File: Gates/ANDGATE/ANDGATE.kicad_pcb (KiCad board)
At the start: 2 copper layers, 53.3 x 20.3 mm, 14 parts, among them J1 Conn_01x01_Socket, J2 Conn_01x01_Socket, J3 Conn_01x03_Socket, U1 SN74LVC1G32DBVR

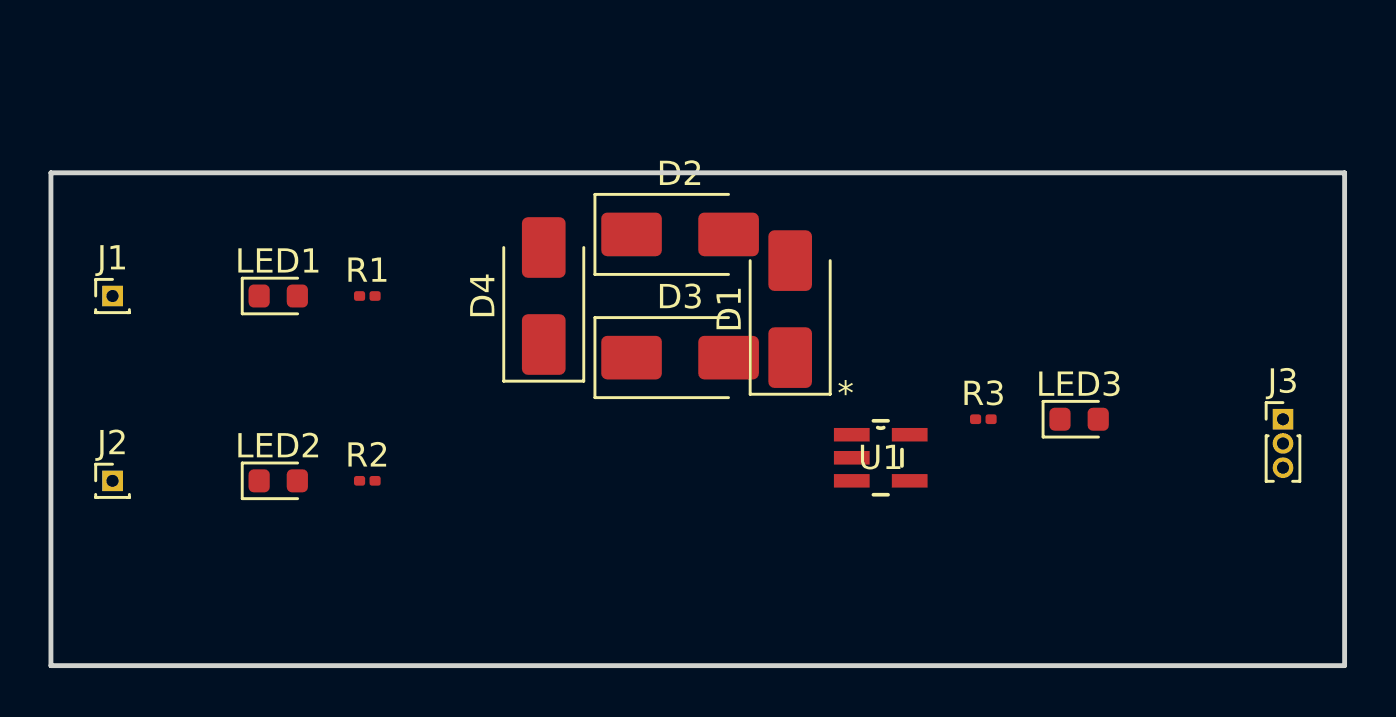
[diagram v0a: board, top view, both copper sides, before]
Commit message: AND GATE passes DRC but with silk screen warnings
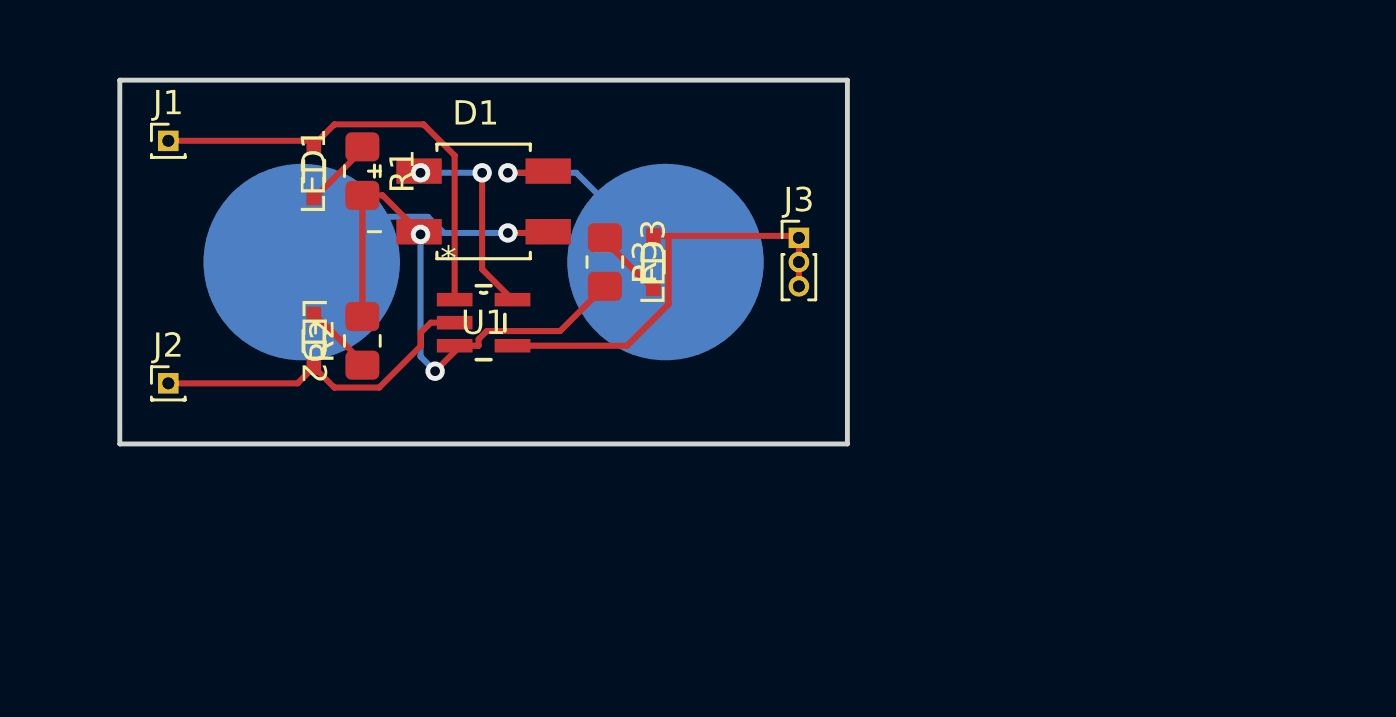
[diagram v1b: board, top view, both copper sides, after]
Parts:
- removed D2, D3, D4: 1N4004, Diode_SMD:D_SMA
- added J4: ~, DigitalLogicFootprints:8mm-snap, B.Cu at (147.5, 87.5)
- added J5: ~, DigitalLogicFootprints:8mm-snap, B.Cu at (162.5, 87.5)
- D1: value 1N4004 -> MB10F-13; footprint Diode_SMD:D_SMA -> DigitalLogicFootprints:DIOB_MB10F-13
- LED1, LED2, LED3: footprint LED_SMD:LED_0603_1608Metric -> DigitalLogicFootprints:LED_LTST-S220GKT_LTO
- R1, R2, R3: footprint Resistor_SMD:R_0201_0603Metric -> Resistor_SMD:R_0805_2012Metric_Pad1.20x1.40mm_HandSolder
- moved J3 21.3 mm to (168.0, 86.5)
- moved LED3 18.7 mm to (162.0, 87.5), turned to 90 degrees
- moved U1 17.3 mm to (155.0, 90.0)
- moved R3 16.9 mm to (160.0, 87.5), turned to -90 degrees
- moved D1 13.4 mm to (155.0, 85.0), turned to 0 degrees
- moved J1 6.80 mm to (142.0, 82.5)
- moved LED2 5.95 mm to (148.0, 90.8), turned to -90 degrees
- moved R2 5.77 mm to (150.0, 90.8), turned to 90 degrees
- moved LED1 5.36 mm to (148.0, 83.8), turned to 90 degrees
- moved R1 5.15 mm to (150.0, 83.8), turned to -90 degrees
- moved J2 4.63 mm to (142.0, 92.5)
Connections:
- D1 pad 1: Net-(D1-K) -> VCC
- D1 pad 2: VCC -> Net-(J5-PWR)
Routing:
- net GND: track 0.00 -> 23.1 mm, vias 0 -> 2
- net Net-(J3-Pin_1): track 0.00 -> 18.9 mm
- net Net-(J1-Pin_1): track 0.00 -> 18.7 mm
- net Net-(J2-Pin_1): track 0.00 -> 13.9 mm
- net Net-(J4-PWR): track 0.00 -> 11.3 mm, vias 0 -> 1
- net Net-(J5-PWR): track 0.00 -> 9.72 mm, vias 0 -> 1
- net VCC: track 0.00 -> 8.29 mm, vias 0 -> 2
- net Net-(LED3-Pad1): track 0.00 -> 2.94 mm
- net Net-(LED2-Pad1): track 0.00 -> 2.94 mm
- net Net-(LED1-Pad1): track 0.00 -> 2.94 mm
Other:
- board size 53.3 x 20.3 mm -> 30 x 15 mm

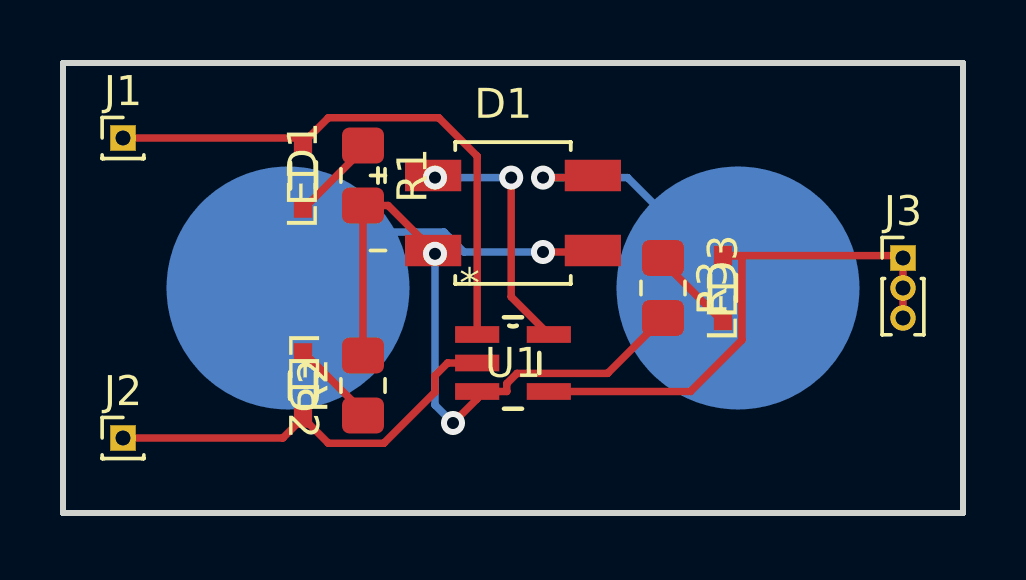
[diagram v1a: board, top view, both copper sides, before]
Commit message: Added mounting holes
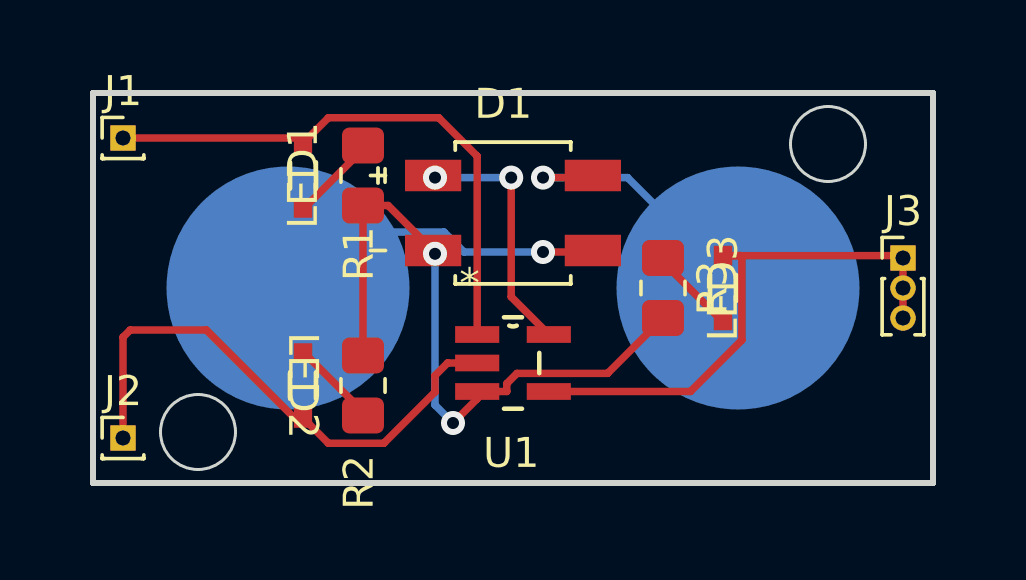
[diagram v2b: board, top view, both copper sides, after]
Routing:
- net Net-(J2-Pin_1): track 13.9 -> 18.3 mm
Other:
- board size 30 x 15 mm -> 28 x 13 mm
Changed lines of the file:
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@@
     (property "ki_keywords" "R res resistor")
     (attr smd)
-    (fp_text reference "R1" (at 0 -1.65 90) (layer "F.SilkS")
-        (effects (font (size 1 1) (thickness 0.15)))
-    )
-    (fp_text value "4k" (at 0 1.65 90) (layer "F.Fab")
+    (fp_text reference "R1" (at 2.61 0.14 90) (layer "F.SilkS")
+        (effects (font (size 1 1) (thickness 0.15)))
+    )
+    (fp_text value "4k" (at -5.01 0.14 90) (layer "F.Fab")
         (effects (font (size 1 1) (thickness 0.15)))
     )
@@
     (property "ki_keywords" "R res resistor")
     (attr smd)
-    (fp_text reference "R2" (at 0 -1.65 90) (layer "F.SilkS")
-        (effects (font (size 1 1) (thickness 0.15)))
-    )
-    (fp_text value "4k" (at 0 1.65 90) (layer "F.Fab")
+    (fp_text reference "R2" (at -3.23 -0.14 90) (layer "F.SilkS")
+        (effects (font (size 1 1) (thickness 0.15)))
+    )
+    (fp_text value "4k" (at 1.85 -0.14 90) (layer "F.Fab")
         (effects (font (size 1 1) (thickness 0.15)))
     )
@@
     (property "ki_keywords" "SN74LVC1G32DBVR")
     (attr smd)
-    (fp_text reference "U1" (at 0 0 unlocked) (layer "F.SilkS")
-        (effects (font (size 1 1) (thickness 0.15)))
-    )
-    (fp_text value "SN74LVC1G32DBVR" (at 0 0 unlocked) (layer "F.Fab")
+    (fp_text reference "U1" (at -0.06 3 unlocked) (layer "F.SilkS")
+        (effects (font (size 1 1) (thickness 0.15)))
+    )
+    (fp_text value "SN74LVC1G32DBVR" (at -0.06 6.52 unlocked) (layer "F.Fab")
         (effects (font (size 1 1) (thickness 0.15)))
     )
@@
     )
     (fp_text user "*" (at -1.4478 -2.6518 unlocked) (layer "F.Fab")
-        (effects (font (size 1 1) (thickness 0.15)))
-    )
-    (fp_text user "${REFERENCE}" (at 0 0 unlocked) (layer "F.Fab")
         (effects (font (size 1 1) (thickness 0.15)))
     )
@@
       (net 9 "Net-(J5-PWR)") (pinfunction "PWR") (pintype "output"))
   )
-  (gr_rect locked (start 140 80) (end 170 95)
+  (gr_circle (center 165.1 81.28) (end 165.1 81.28)
+    (stroke (width 0.1) (type default)) (fill none) (layer "Edge.Cuts"))
+  (gr_rect locked (start 141 81) (end 169 94)
     (stroke (width 0.2) (type default)) (fill none) (layer "Edge.Cuts"))
+  (gr_circle (center 165.5 82.7) (end 166.75 82.7)
+    (stroke (width 0.1) (type default)) (fill none) (layer "Edge.Cuts"))
+  (gr_circle (center 144.5 92.3) (end 145.75 92.3)
+    (stroke (width 0.1) (type default)) (fill none) (layer "Edge.Cuts"))
   (segment (start 150 84.75) (end 150 89.75) (width 0.25) (layer "F.Cu") (net 1))
   (segment (start 152.4475 86.36) (end 150.8375 84.75) (width 0.25) (layer "F.Cu") (net 1))
@@
   (via (at 153 92) (size 0.8) (drill 0.4) (layers "F.Cu" "B.Cu") (free) (net 1))
   (via (at 152.4 86.36) (size 0.8) (drill 0.4) (layers "F.Cu" "B.Cu") (net 1))
-  (segment (start 153 92) (end 152.4 91.4) (width 0.25) (layer "B.Cu") (net 1))
-  (segment (start 152.4 91.4) (end 152.4 86.36) (width 0.25) (layer "B.Cu") (net 1))
+  (segment (start 152.4 91.4) (end 153 92) (width 0.25) (layer "B.Cu") (net 1))
+  (segment (start 152.4 86.36) (end 152.4 91.4) (width 0.25) (layer "B.Cu") (net 1))
   (segment (start 154.94 87.796199) (end 154.94 83.82) (width 0.25) (layer "F.Cu") (net 2))
   (segment (start 156.1938 89.049999) (end 154.94 87.796199) (width 0.25) (layer "F.Cu") (net 2))
@@
   (segment (start 142 82.5) (end 147.8295 82.5) (width 0.25) (layer "F.Cu") (net 6))
   (segment (start 148 82.6705) (end 148.8455 81.825) (width 0.25) (layer "F.Cu") (net 6))
+  (segment (start 147.7095 91.8295) (end 148 91.8295) (width 0.25) (layer "F.Cu") (net 7))
+  (segment (start 147.7095 91.8295) (end 144.78 88.9) (width 0.25) (layer "F.Cu") (net 7))
   (segment (start 152.4 90.4196) (end 152.4 90.9701) (width 0.25) (layer "F.Cu") (net 7))
   (segment (start 152.4 90.9701) (end 150.6951 92.675) (width 0.25) (layer "F.Cu") (net 7))
+  (segment (start 142 89.14) (end 142 92.5) (width 0.25) (layer "F.Cu") (net 7))
   (segment (start 153.8062 90) (end 152.8196 90) (width 0.25) (layer "F.Cu") (net 7))
   (segment (start 152.8196 90) (end 152.4 90.4196) (width 0.25) (layer "F.Cu") (net 7))
-  (segment (start 147.3295 92.5) (end 148 91.8295) (width 0.25) (layer "F.Cu") (net 7))
   (segment (start 148.8455 92.675) (end 148 91.8295) (width 0.25) (layer "F.Cu") (net 7))
   (segment (start 150.6951 92.675) (end 148.8455 92.675) (width 0.25) (layer "F.Cu") (net 7))
-  (segment (start 142 92.5) (end 147.3295 92.5) (width 0.25) (layer "F.Cu") (net 7))
+  (segment (start 142.24 88.9) (end 142 89.14) (width 0.25) (layer "F.Cu") (net 7))
+  (segment (start 144.78 88.9) (end 142.24 88.9) (width 0.25) (layer "F.Cu") (net 7))
   (segment (start 160.914499 90.950001) (end 156.1938 90.950001) (width 0.25) (layer "F.Cu") (net 8))
   (segment (start 162.6298 86.4955) (end 162.6298 89.2347) (width 0.25) (layer "F.Cu") (net 8))

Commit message: Added HBB logo
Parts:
- added G***: LOGO, DigitalLogicFootprints:HBBLogo, F.Cu at (167.0, 93.0)

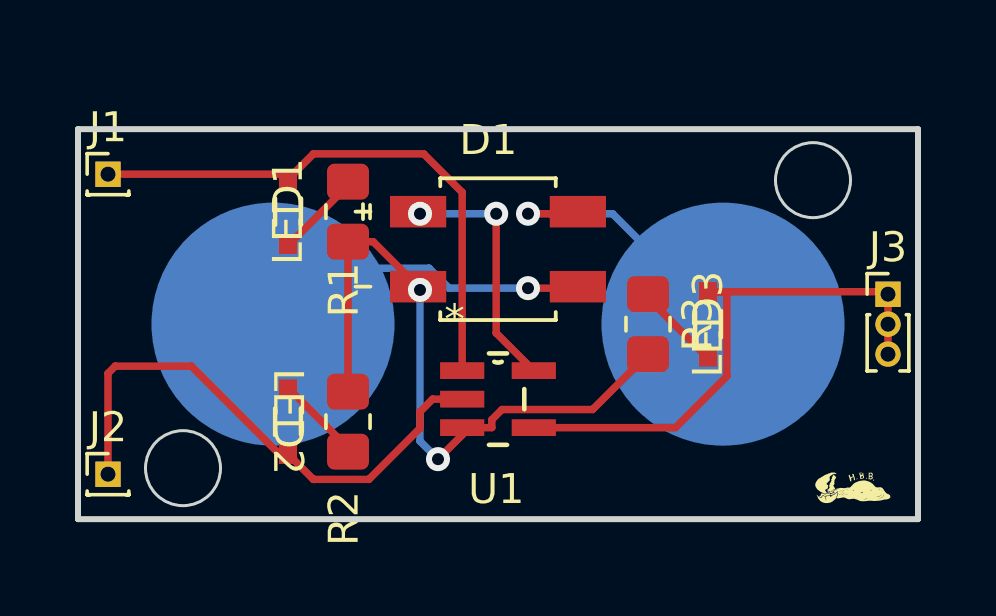
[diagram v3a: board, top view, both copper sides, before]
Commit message: Changed pins to 2.54mm from 1mm
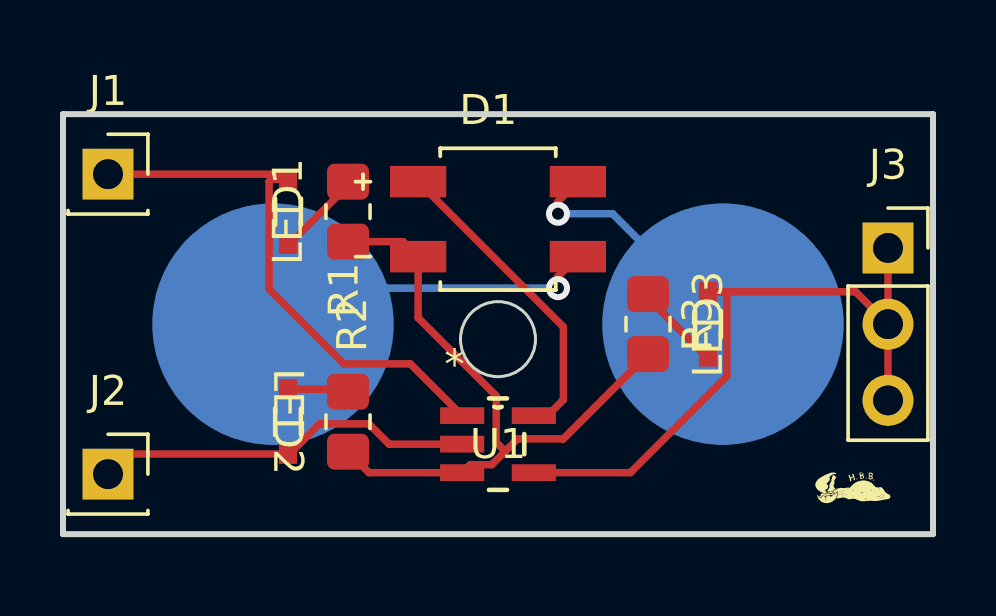
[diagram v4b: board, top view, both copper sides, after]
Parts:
- J1, J2: footprint Connector_PinHeader_1.00mm:PinHeader_1x01_P1.00mm_Vertical -> Connector_PinSocket_2.54mm:PinSocket_1x01_P2.54mm_Vertical
- J3: footprint Connector_PinHeader_1.00mm:PinHeader_1x03_P1.00mm_Vertical -> Connector_PinSocket_2.54mm:PinSocket_1x03_P2.54mm_Vertical
- moved J3 1.54 mm to (168.0, 85.0)
- moved U1 1.50 mm to (155.0, 91.5)
- moved D1 1.00 mm to (155.0, 84.0)
- turned R2 to -90 degrees
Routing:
- net Net-(J2-Pin_1): track 18.3 -> 12.8 mm
- net Net-(J3-Pin_1): track 18.9 -> 22.9 mm
- net Net-(J4-PWR): track 11.3 -> 14.0 mm
- net VCC: track 8.29 -> 10.5 mm, vias 2 -> 0
- net Net-(J5-PWR): track 9.72 -> 8.37 mm
- net Net-(LED2-Pad1): track 2.94 -> 2.03 mm
- net GND: track 23.1 -> 22.4 mm, vias 2 -> 0
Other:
- board size 28 x 13 mm -> 29 x 14 mm

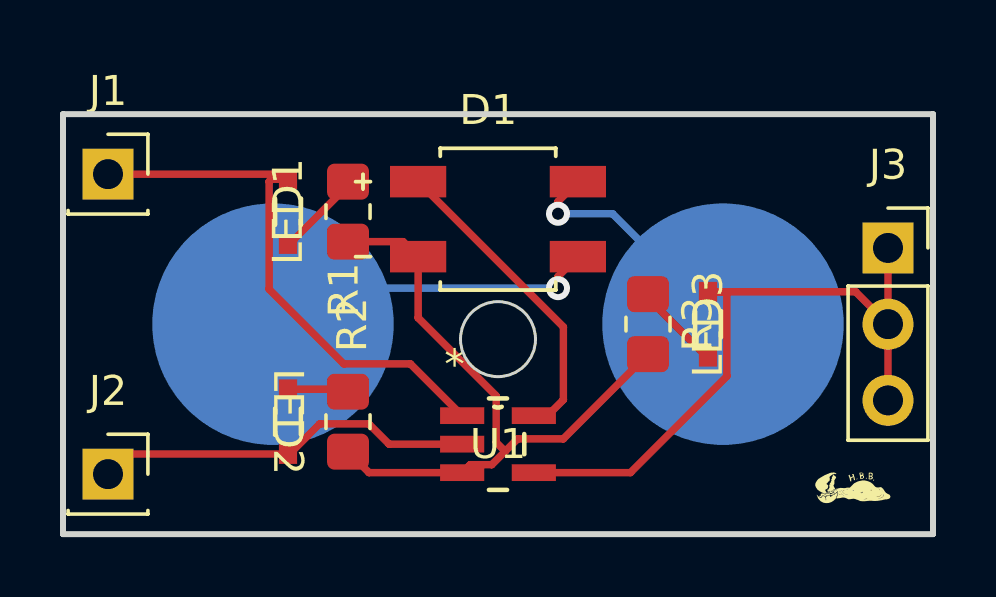
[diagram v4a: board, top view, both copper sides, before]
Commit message: AND Gate Inventor 3D casing
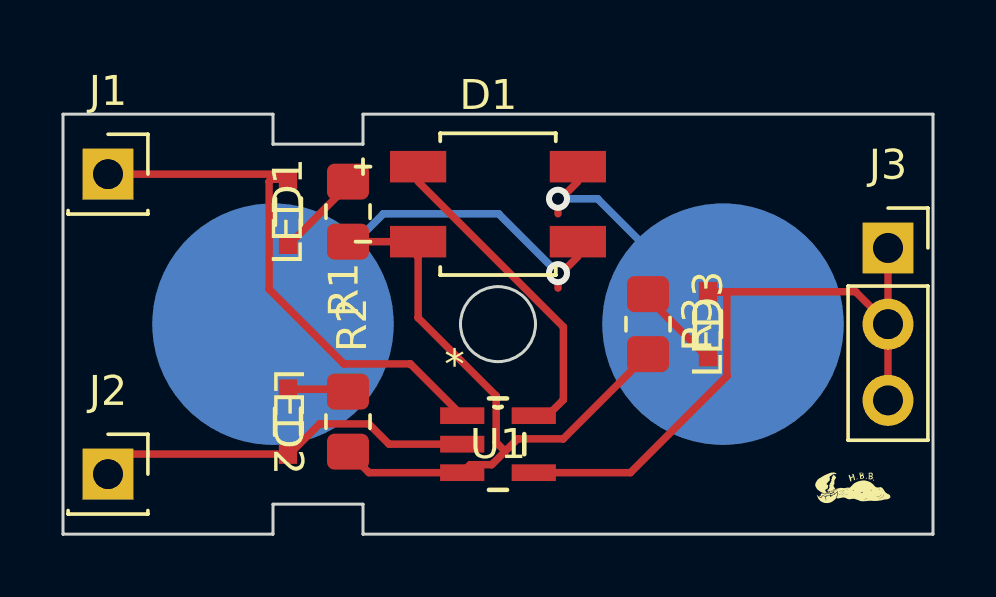
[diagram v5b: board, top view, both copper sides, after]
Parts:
- moved D1 0.50 mm to (155.0, 83.5)
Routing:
- net Net-(J4-PWR): track 14.0 -> 15.8 mm
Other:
- outline, holes or cut-outs redrawn
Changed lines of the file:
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@@
   )
   (footprint "DigitalLogicFootprints:DIOB_MB10F-13" (layer "F.Cu")
-    (at 155 84)
+    (at 155 83.5)
     (property "Availability" "In Stock")
     (property "Check_prices" "https://www.snapeda.com/parts/MB10F-13/Zetex/view-part/?ref=eda")
@@
       (net 9 "Net-(J5-PWR)") (pinfunction "PWR") (pintype "output"))
   )
+  (gr_poly
+    (pts
+      (xy 140.5 80.5)
+      (xy 147.5 80.5)
+      (xy 147.5 81.5)
+      (xy 150.5 81.5)
+      (xy 150.5 80.5)
+      (xy 169.5 80.5)
+      (xy 169.5 94.5)
+      (xy 150.5 94.5)
+      (xy 150.5 93.5)
+      (xy 147.5 93.5)
+      (xy 147.5 94.5)
+      (xy 140.5 94.5)
+    )
+    (stroke (width 0.1) (type solid)) (fill none) (layer "Edge.Cuts"))
   (gr_circle (center 165.1 81.28) (end 165.1 81.28)
     (stroke (width 0.1) (type default)) (fill none) (layer "Edge.Cuts"))
-  (gr_rect (start 140.5 80.5) (end 169.5 94.5)
-    (stroke (width 0.2) (type default)) (fill none) (layer "Edge.Cuts"))
-  (gr_circle (center 155 88) (end 156.25 88)
+  (gr_circle (center 155 87.5) (end 156.25 87.5)
     (stroke (width 0.1) (type default)) (fill none) (layer "Edge.Cuts"))
   (segment (start 155.653749 91.324052) (end 157.175948 91.324052) (width 0.25) (layer "F.Cu") (net 1))
@@
   (segment (start 157 83.82) (end 157 83.4125) (width 0.25) (layer "F.Cu") (net 9))
   (segment (start 157 83.4125) (end 157.6625 82.75) (width 0.25) (layer "F.Cu") (net 9))
-  (via (at 157 83.82) (size 0.8) (drill 0.4) (layers "F.Cu" "B.Cu") (net 9))
-  (segment (start 158.82 83.82) (end 162.5 87.5) (width 0.25) (layer "B.Cu") (net 9))
-  (segment (start 157 83.82) (end 158.82 83.82) (width 0.25) (layer "B.Cu") (net 9))
+  (via (at 157 83.32) (size 0.8) (drill 0.4) (layers "F.Cu" "B.Cu") (net 9))
+  (segment (start 157 83.32) (end 158.32 83.32) (width 0.25) (layer "B.Cu") (net 9))
+  (segment (start 158.32 83.32) (end 162.5 87.5) (width 0.25) (layer "B.Cu") (net 9))
   (segment (start 157 86.3) (end 157 85.9125) (width 0.25) (layer "F.Cu") (net 10))
   (segment (start 157 85.9125) (end 157.6625 85.25) (width 0.25) (layer "F.Cu") (net 10))
-  (via (at 157 86.3) (size 0.8) (drill 0.4) (layers "F.Cu" "B.Cu") (net 10))
-  (segment (start 148.7 86.3) (end 147.5 87.5) (width 0.25) (layer "B.Cu") (net 10))
-  (segment (start 157 86.3) (end 148.7 86.3) (width 0.25) (layer "B.Cu") (net 10))
+  (via (at 157 85.8) (size 0.8) (drill 0.4) (layers "F.Cu" "B.Cu") (net 10))
+  (segment (start 155.02 83.82) (end 151.18 83.82) (width 0.25) (layer "B.Cu") (net 10))
+  (segment (start 157 85.8) (end 155.02 83.82) (width 0.25) (layer "B.Cu") (net 10))
+  (segment (start 151.18 83.82) (end 147.5 87.5) (width 0.25) (layer "B.Cu") (net 10))
   (segment (start 149.365 85.635) (end 147.5 87.5) (width 0.25) (layer "B.Cu") (net 10))
 )
